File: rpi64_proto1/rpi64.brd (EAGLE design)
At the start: 100 x 80 mm, 113 parts, among them Q1 BSS123, Q2 BSS123

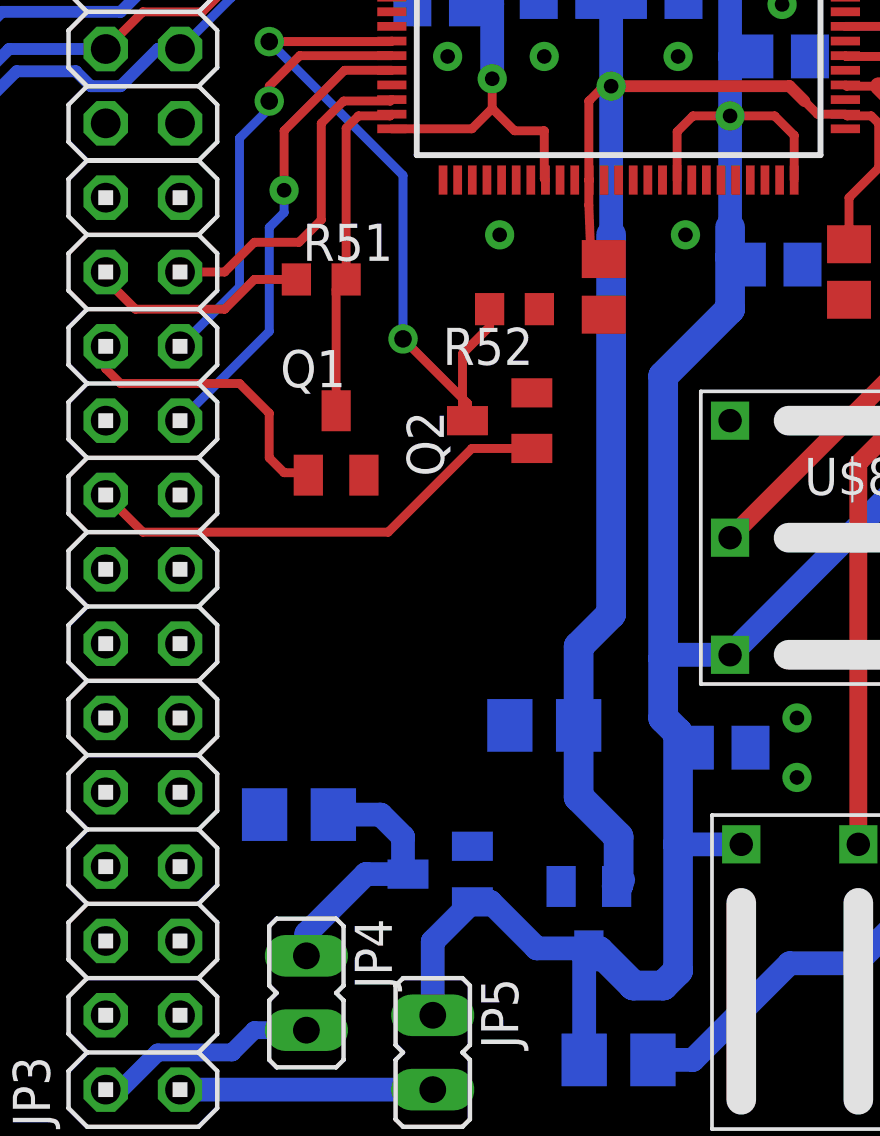
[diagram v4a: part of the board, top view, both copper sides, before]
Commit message: Added clocks
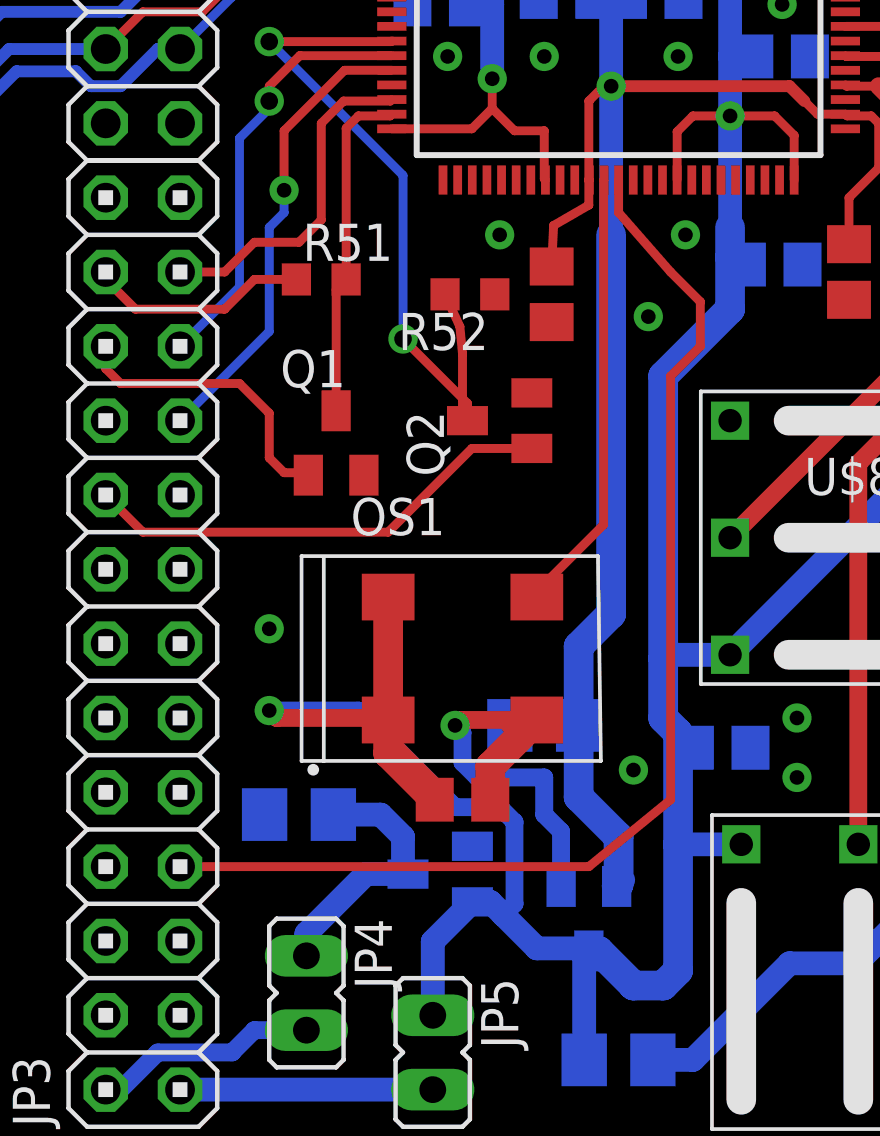
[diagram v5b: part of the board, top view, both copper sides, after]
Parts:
- added C16: (no value), rcl:C0805
- added OS1: OSC-OE-CFPS-73, IQD-Frequency-Products:7.2X5.2-4-PAD
- moved C11 1.80 mm to (83.8, 29.0)
- moved R52 1.61 mm to (81.0, 29.0)
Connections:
- new net OSC_OUT: OS1.3, U$2.62
- new net RPI_CLKOUT: JP3.7, U$2.63
- net +3V3: now also C16.1, OS1.1, OS1.4
- net GND: now also C16.2, OS1.2
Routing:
- net RPI_CLKOUT: track 0.00 -> 40.3 mm
- net +3V3: track 209.0 -> 237.4 mm, vias 10 -> 11
- net GND: track 44.2 -> 60.3 mm, vias 16 -> 20
- net OSC_OUT: track 0.00 -> 15.2 mm
- net V1V2: track 75.1 -> 75.7 mm

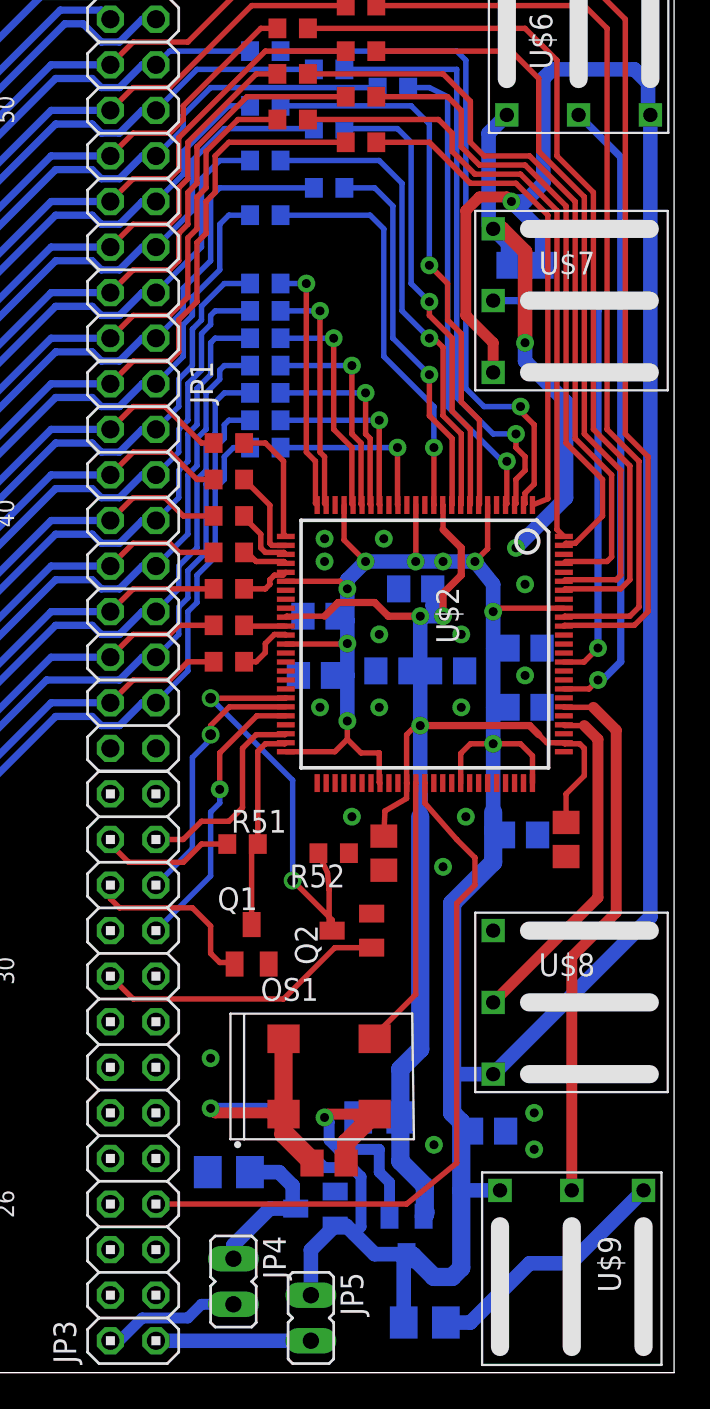
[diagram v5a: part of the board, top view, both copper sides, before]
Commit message: Everything placed and routed
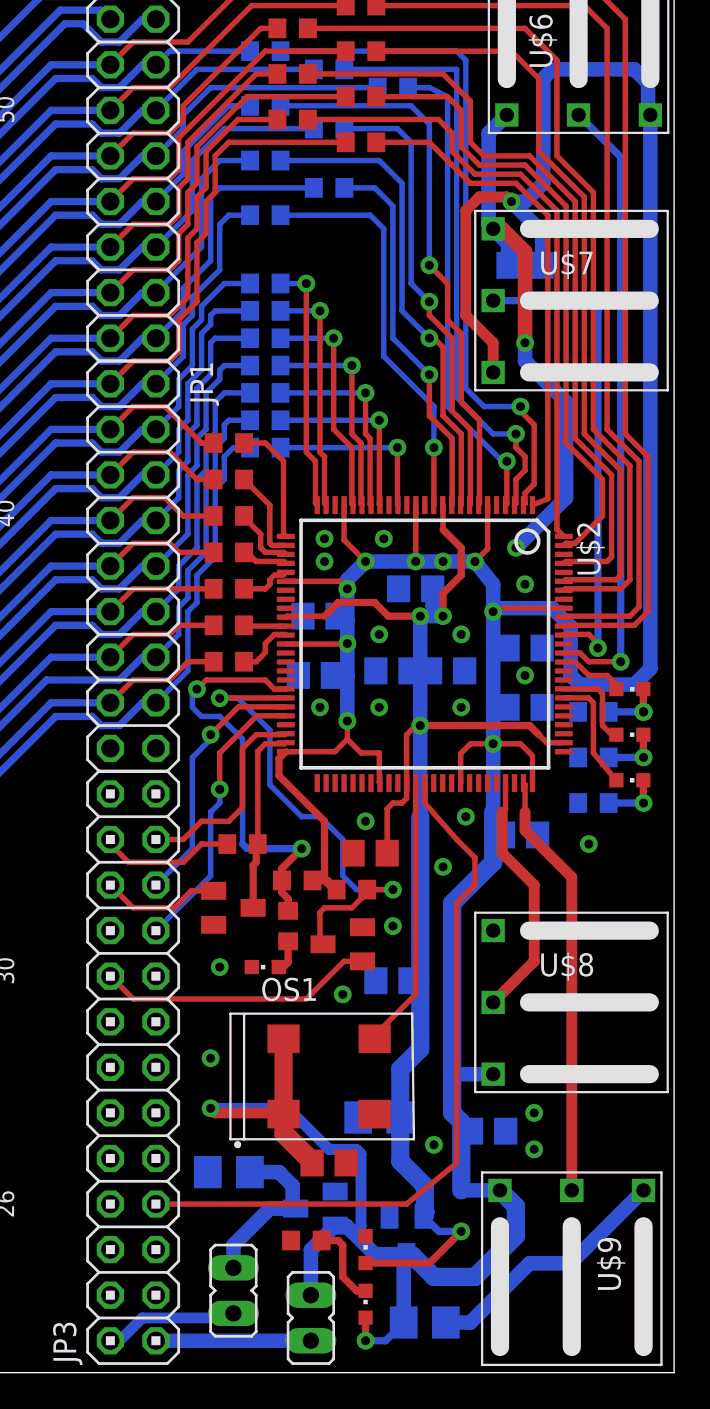
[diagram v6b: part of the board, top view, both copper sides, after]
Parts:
- added LED1, LED2, LED3, LED5, LED6, LED7: (no value), led:CHIPLED_0603
- added R68, R69: 1k, rcl:R0603
- added R70, R88, R89, R90: (no value), rcl:R0603
- moved C10 12.5 mm to (84.3, 21.8), flipped to the bottom, turned to 0 degrees
- moved R52 2.27 mm to (82.0, 26.9), turned to 0 degrees
- moved Q1 2.27 mm to (75.4, 25.9), turned to 270 degrees
- moved Q2 0.92 mm to (81.5, 23.9)
- moved C11 0.76 mm to (83.1, 29.0), turned to 180 degrees
- moved JP4 0.51 mm to (75.4, 4.57)
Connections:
- new net LED0: U$2.80
- new net LED1: LED5.A, U$2.82
- new net LED2: LED6.A, U$2.83
- new net LED3: LED7.A, U$2.86
- new net N$104: LED1.A, R69.2
- new net N$107: LED7.C, R90.1
- new net N$109: LED6.C, R89.1
- new net N$111: LED5.C, R88.1
- new net N$116: LED2.C, R70.1
- new net N$91: R68.1, R69.1, U$2.43
- net +3V3: now also LED2.A, R68.2
- net CTRL0: now also U$2.87; no longer U$2.83
- net CTRL1: now also U$2.89; no longer U$2.86
- net CTRL2: now also U$2.72; no longer U$2.79
- net CTRL3: now also U$2.74; no longer U$2.81
- net GND: now also LED1.C, LED3.C, R70.2, R88.2, R89.2, R90.2
- net V1V2: now also LED3.A
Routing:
- net N$91: track 0.00 -> 23.3 mm, vias 0 -> 2
- net GND: track 60.3 -> 45.0 mm, vias 20 -> 23
- net LED1: track 0.00 -> 6.57 mm
- net CTRL3: track 30.1 -> 23.8 mm
- net LED2: track 0.00 -> 5.40 mm
- net CTRL2: track 19.3 -> 14.0 mm
- net N$116: track 0.00 -> 4.66 mm
- net V1V2: track 75.7 -> 80.0 mm, vias 3 -> 4
- net +3V3: track 237.4 -> 241.5 mm, vias 11 -> 12
- net LED3: track 0.00 -> 3.70 mm
- net RPI_GPIO25: track 10.1 -> 6.68 mm
- net N$111: track 0.00 -> 3.22 mm, vias 0 -> 1
- net N$109: track 0.00 -> 3.22 mm, vias 0 -> 1
- net N$107: track 0.00 -> 3.22 mm, vias 0 -> 2
- net N$103: track 24.5 -> 27.2 mm
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
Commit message: Resolved DRC problems
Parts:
- moved U$3 0.13 mm to (0.38, 70.1)
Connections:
- removed net N$110: U$2.96
- removed net N$113: U$2.15
- removed net N$114: U$2.13
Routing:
- net SLOT_21: track 14.0 -> 15.2 mm
- net SLOT_18: track 12.0 -> 12.9 mm
- net SLOT_20: track 13.2 -> 14.0 mm
- net SLOT_19: track 12.7 -> 13.5 mm
- net N$76: track 60.9 -> 60.2 mm
- net SLOT_17: track 11.1 -> 11.8 mm
- net N$107: vias 2 -> 1
- net GND: vias 23 -> 24
- added copper zone on layer 1, net GND
- added copper zone on layer 16, net GND

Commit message: First prototype
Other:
- board size 100 x 80 mm -> 99.7 x 80 mm
- board text added: "JAN MARJANOVIC, 2015"
- board text added: "MARJANOVIC 2015"
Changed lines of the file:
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@@
 <setting verticaltext="up"/>
 </settings>
-<grid distance="0.001" unitdist="inch" unit="inch" style="lines" multiple="1" display="yes" altdistance="0.05" altunitdist="inch" altunit="inch"/>
+<grid distance="2.54" unitdist="mm" unit="mm" style="lines" multiple="1" display="yes" altdistance="0.05" altunitdist="inch" altunit="inch"/>
 <layers>
 <layer number="1" name="Top" color="4" fill="1" visible="yes" active="yes"/>
@@
 <board>
 <plain>
-<wire x1="0" y1="0" x2="100" y2="0" width="0" layer="20"/>
+<wire x1="46.99" y1="0" x2="100" y2="0" width="0" layer="20"/>
 <wire x1="100" y1="0" x2="100" y2="80" width="0" layer="20"/>
-<wire x1="100" y1="80" x2="0" y2="80" width="0" layer="20"/>
-<wire x1="0" y1="80" x2="0" y2="0" width="0" layer="20"/>
-<dimension x1="0" y1="80" x2="6.858" y2="72.898" x3="-2.54" y3="76.449" textsize="1.778" layer="20" dtype="vertical"/>
-<dimension x1="3.556" y1="7.366" x2="4.064" y2="0.254" x3="-4.826" y3="3.81" textsize="1.778" layer="20" dtype="vertical"/>
-<dimension x1="101.092" y1="11.176" x2="101.092" y2="15.24" x3="102.616" y3="13.208" textsize="1.778" layer="20" dtype="vertical"/>
-<dimension x1="101.092" y1="25.908" x2="101.092" y2="29.972" x3="102.616" y3="27.94" textsize="1.778" layer="20" dtype="vertical"/>
-<dimension x1="100.584" y1="65.024" x2="100.584" y2="69.088" x3="102.108" y3="67.056" textsize="1.778" layer="20" dtype="vertical"/>
-<dimension x1="100.584" y1="50.292" x2="100.584" y2="54.356" x3="102.108" y3="52.324" textsize="1.778" layer="20" dtype="vertical"/>
-<dimension x1="89.408" y1="80.518" x2="85.344" y2="80.518" x3="87.376" y3="84.836" textsize="1.778" layer="20" dtype="horizontal"/>
-<dimension x1="0" y1="80" x2="50.038" y2="80.01" x3="25.019" y3="84.328" textsize="1.778" layer="20" dtype="horizontal"/>
-<dimension x1="84.836" y1="-0.508" x2="88.9" y2="-0.508" x3="86.868" y3="-4.826" textsize="1.778" layer="20" dtype="horizontal"/>
+<wire x1="100" y1="80" x2="46.99" y2="80" width="0" layer="20"/>
+<wire x1="46.99" y1="80" x2="46.99" y2="72.644" width="0" layer="20"/>
+<wire x1="46.99" y1="72.644" x2="0.254" y2="72.644" width="0" layer="20"/>
+<wire x1="0.254" y1="72.644" x2="0.254" y2="7.366" width="0" layer="20"/>
+<wire x1="0.254" y1="7.366" x2="46.99" y2="7.366" width="0" layer="20"/>
+<wire x1="46.99" y1="7.366" x2="46.99" y2="0" width="0" layer="20"/>
+<text x="75.5142" y="62.2808" size="1.27" layer="21">MARJANOVIC
+        2015</text>
+<text x="40.0304" y="65.024" size="3.048" layer="21" rot="SR270">JAN MARJANOVIC, 2015</text>
+<text x="40.0304" y="65.024" size="3.048" layer="21" rot="SR270">JAN MARJANOVIC, 2015</text>
+<text x="43.1546" y="65.024" size="3.048" layer="22" rot="SMR270">JAN MARJANOVIC, 2015</text>
 </plain>
 <attributes>
@@
 <contactref element="U$2" pad="94"/>
 <wire x1="79.59" y1="74.93" x2="91.694" y2="74.93" width="0.3048" layer="1"/>
-<wire x1="91.694" y1="74.93" x2="93.472" y2="73.152" width="0.3048" layer="1"/>
+<wire x1="91.694" y1="74.93" x2="93.2434" y2="73.5076" width="0.3048" layer="1"/>
 <wire x1="97.536" y1="50.546" x2="97.536" y2="44.1198" width="0.3048" layer="1"/>
 <wire x1="97.536" y1="44.1198" x2="97.028" y2="43.6118" width="0.3048" layer="1"/>
 <wire x1="97.028" y1="43.6118" x2="93.908884375" y2="43.6118" width="0.3048" layer="1"/>
 <wire x1="93.908884375" y1="43.6118" x2="93.856971875" y2="43.6106875" width="0.3048" layer="1"/>
-<wire x1="93.472" y1="73.152" x2="93.472" y2="67.818" width="0.3048" layer="1"/>
-<wire x1="93.472" y1="67.818" x2="95.504" y2="65.786" width="0.3048" layer="1"/>
+<wire x1="93.2434" y1="73.5076" x2="93.218" y2="68.0974" width="0.3048" layer="1"/>
+<wire x1="93.218" y1="68.0974" x2="95.504" y2="65.786" width="0.3048" layer="1"/>
 <wire x1="95.504" y1="65.786" x2="95.504" y2="52.578" width="0.3048" layer="1"/>
 <wire x1="95.504" y1="52.578" x2="97.536" y2="50.546" width="0.3048" layer="1"/>
@@
 </board>
 </drawing>
+<compatibility>
+<note version="6.3" minversion="6.2.2" severity="warning">
+Since Version 6.2.2 text objects can contain more than one line,
+which will not be processed correctly with this version.
+</note>
+</compatibility>
 </eagle>
